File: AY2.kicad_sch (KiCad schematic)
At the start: 5 parts, among them J16 DB9_Pins, U11 74HCT240, U9 74LS32

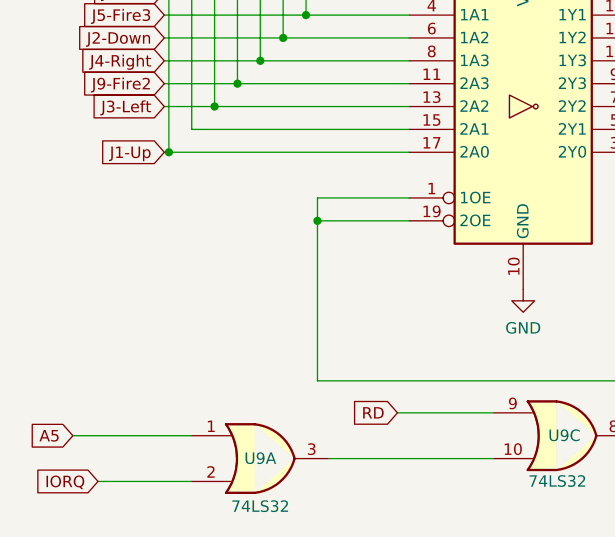
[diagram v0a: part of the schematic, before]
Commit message: Add files via upload
Added optional +/-12V for IF2 Serial support. Only fit if required.
Added jumper J18 to enable/disable Joystick interface ( fitted to enable, remove to disable).
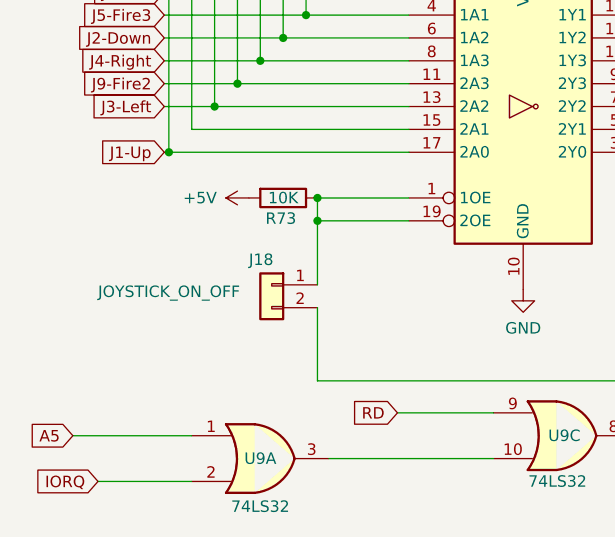
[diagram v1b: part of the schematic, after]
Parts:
- added J18: JOYSTICK_ON_OFF, Connector_PinHeader_2.54mm:PinHeader_1x02_P2.54mm_Vertical, symbol Connector_Generic:Conn_01x02
- added R73: 10K, Resistor_THT:R_Axial_DIN0204_L3.6mm_D1.6mm_P7.62mm_Horizontal, symbol Device:R
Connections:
- net +5V: now also R73.2
- net at U11.1 (1OE), U11.19 (2OE): now also J18.1 (Pin_1), R73.1; no longer U9.8
- new net: J18.2 (Pin_2), U9.8
